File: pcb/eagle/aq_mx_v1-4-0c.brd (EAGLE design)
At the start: 208.6 x 112.5 mm, 38 parts, among them J1 DB9-MALE-RA, J2 DB9-MALE-RA, Q1 BC548, U1 CY62256LL-PC, U2 AY-3-8910, U3 27C512AP, U4 GAL16V8, U5 74LS74N, U6 GAL16V8, U7 74LS244N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

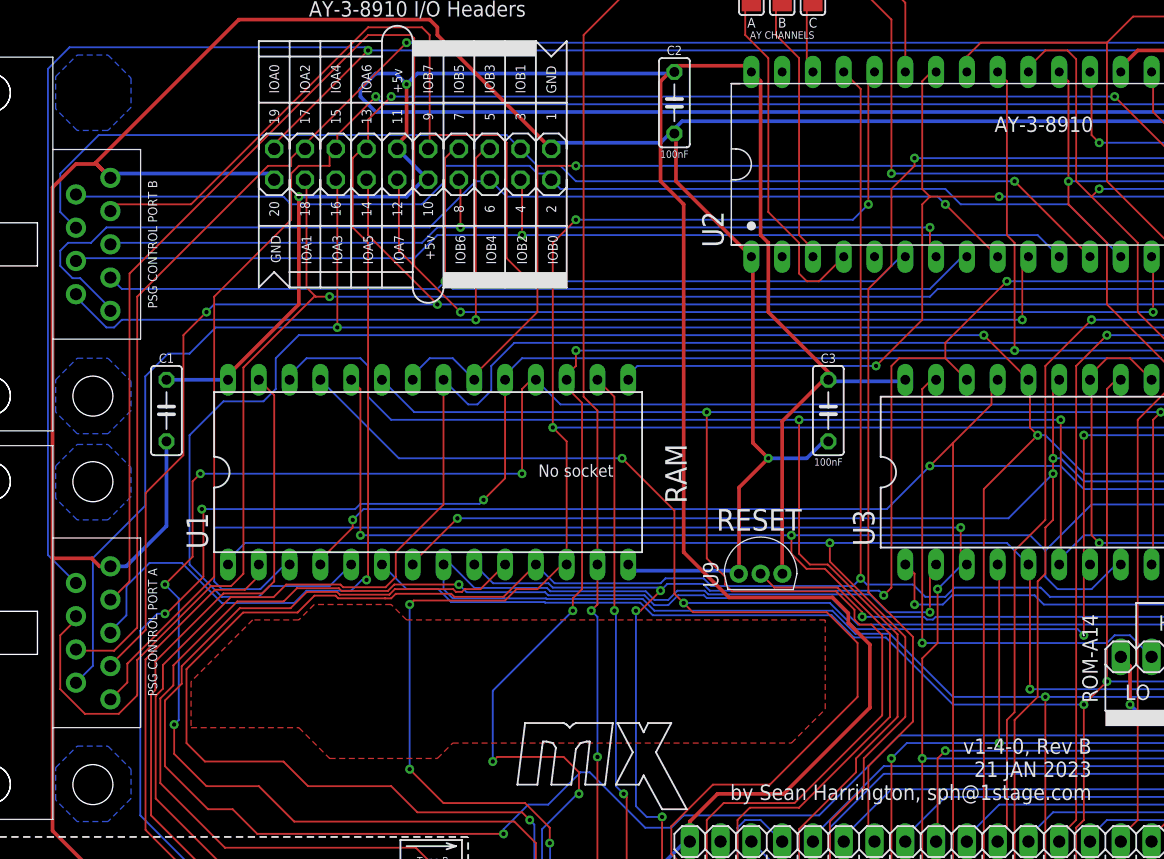
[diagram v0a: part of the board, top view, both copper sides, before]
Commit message: Fix for 1.4.0c PCB
Controller B was missing one of it's mounting holes for metal DB9 ports. If you ordered a PCB with 1.4.0b, you can drill a 1.8" / 3.25mm hole in that position to match the others.
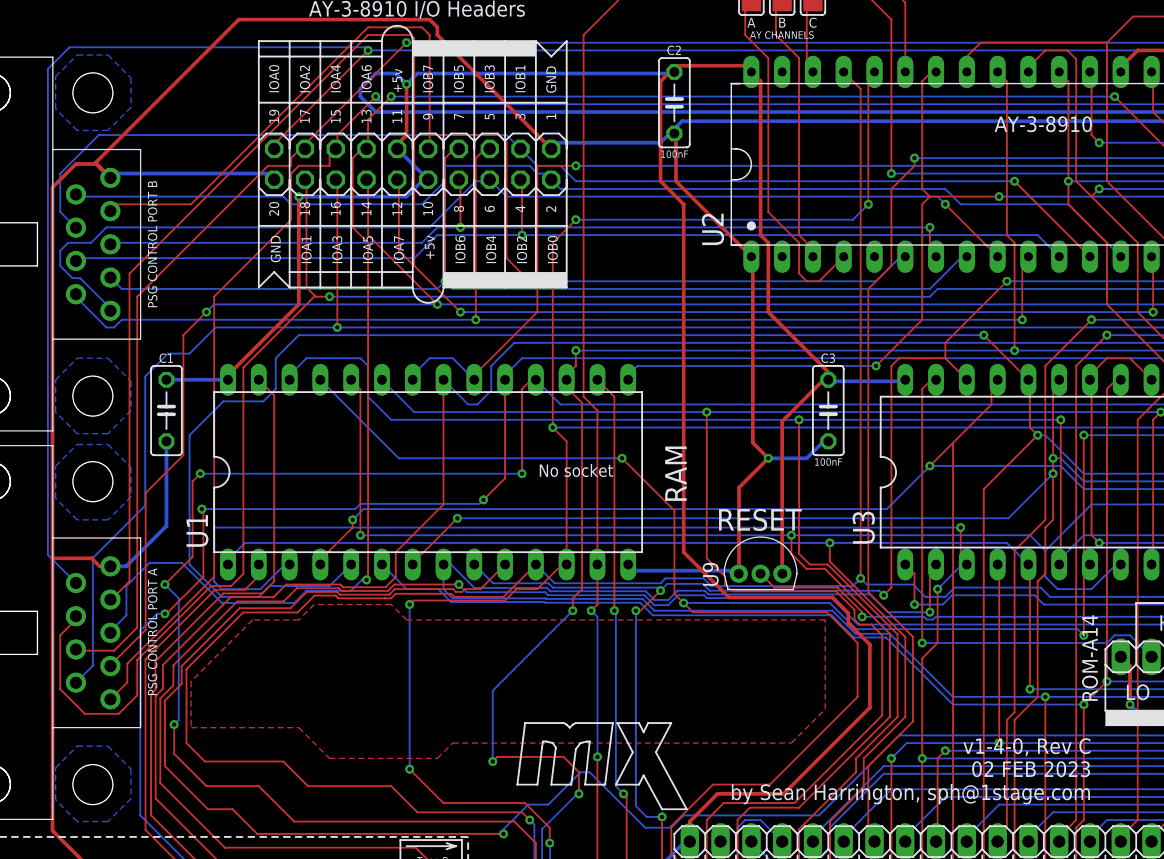
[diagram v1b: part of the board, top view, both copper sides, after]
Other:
- outline, holes or cut-outs redrawn
- board text added: "v1-4-0, Rev C 02 FEB 2023 by Sean Harrington, sph@1stage.com"
- board text removed: "v1-4-0, Rev B 21 JAN 2023 by Sean Harrington, sph@1stage.com"
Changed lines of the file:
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@@
 <grid distance="50" unitdist="mil" unit="mil" style="lines" multiple="1" display="no" altdistance="5" altunitdist="mil" altunit="mil"/>
 <layers>
-<layer number="1" name="Top" color="4" fill="1" visible="yes" active="yes"/>
+<layer number="1" name="Top" color="4" fill="1" visible="no" active="yes"/>
 <layer number="2" name="Route2" color="16" fill="1" visible="no" active="no"/>
 <layer number="3" name="Route3" color="17" fill="1" visible="no" active="no"/>
@@
 <layer number="14" name="Route14" color="22" fill="1" visible="no" active="no"/>
 <layer number="15" name="Route15" color="23" fill="1" visible="no" active="no"/>
-<layer number="16" name="Bottom" color="1" fill="1" visible="yes" active="yes"/>
+<layer number="16" name="Bottom" color="1" fill="1" visible="no" active="yes"/>
 <layer number="17" name="Pads" color="2" fill="1" visible="yes" active="yes"/>
 <layer number="18" name="Vias" color="2" fill="1" visible="yes" active="yes"/>
@@
 <wire x1="133.4262" y1="112.4966" x2="134.6962" y2="111.3536" width="0" layer="20" curve="-90"/>
 <wire x1="134.6962" y1="111.3536" x2="134.7216" y2="98.7044" width="0" layer="20"/>
-<text x="100.965" y="44.831" size="1.27" layer="21" rot="R180" align="center-left">v1-4-0, Rev B
-21 JAN 2023
+<text x="100.965" y="44.831" size="1.27" layer="21" rot="R180" align="center-left">v1-4-0, Rev C
+02 FEB 2023
 by Sean Harrington, sph@1stage.com</text>
 <circle x="10.1854" y="100.6348" radius="1.5748" width="0.0254" layer="20"/>
@@
 <text x="49.911" y="18.288" size="0.6096" layer="21" align="center-left">GND</text>
 <text x="49.911" y="15.748" size="0.6096" layer="21" align="center-left">VCC/5V</text>
-<circle x="18.5674" y="100.6348" radius="1.651" width="0.025" layer="45"/>
+<circle x="18.5674" y="100.6348" radius="1.651" width="0.025" layer="46"/>
 <circle x="18.5674" y="75.6158" radius="1.651" width="0.025" layer="46"/>
 <circle x="18.5674" y="68.5546" radius="1.651" width="0.025" layer="46"/>
